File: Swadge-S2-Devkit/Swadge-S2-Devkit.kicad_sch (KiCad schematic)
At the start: 92 parts, among them J1 LED, J2 DEBUG, P1 USB_C_Plug_USB2.0, Q1 PMOS, SW1 TS-1109S-A-A, SW2 TS-1109S-A-A, SW3 TS-1109S-A-A, SW4 TS-1109S-A-A, SW5 TS-1109S-A-A, SW6 TS-1109S-A-A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

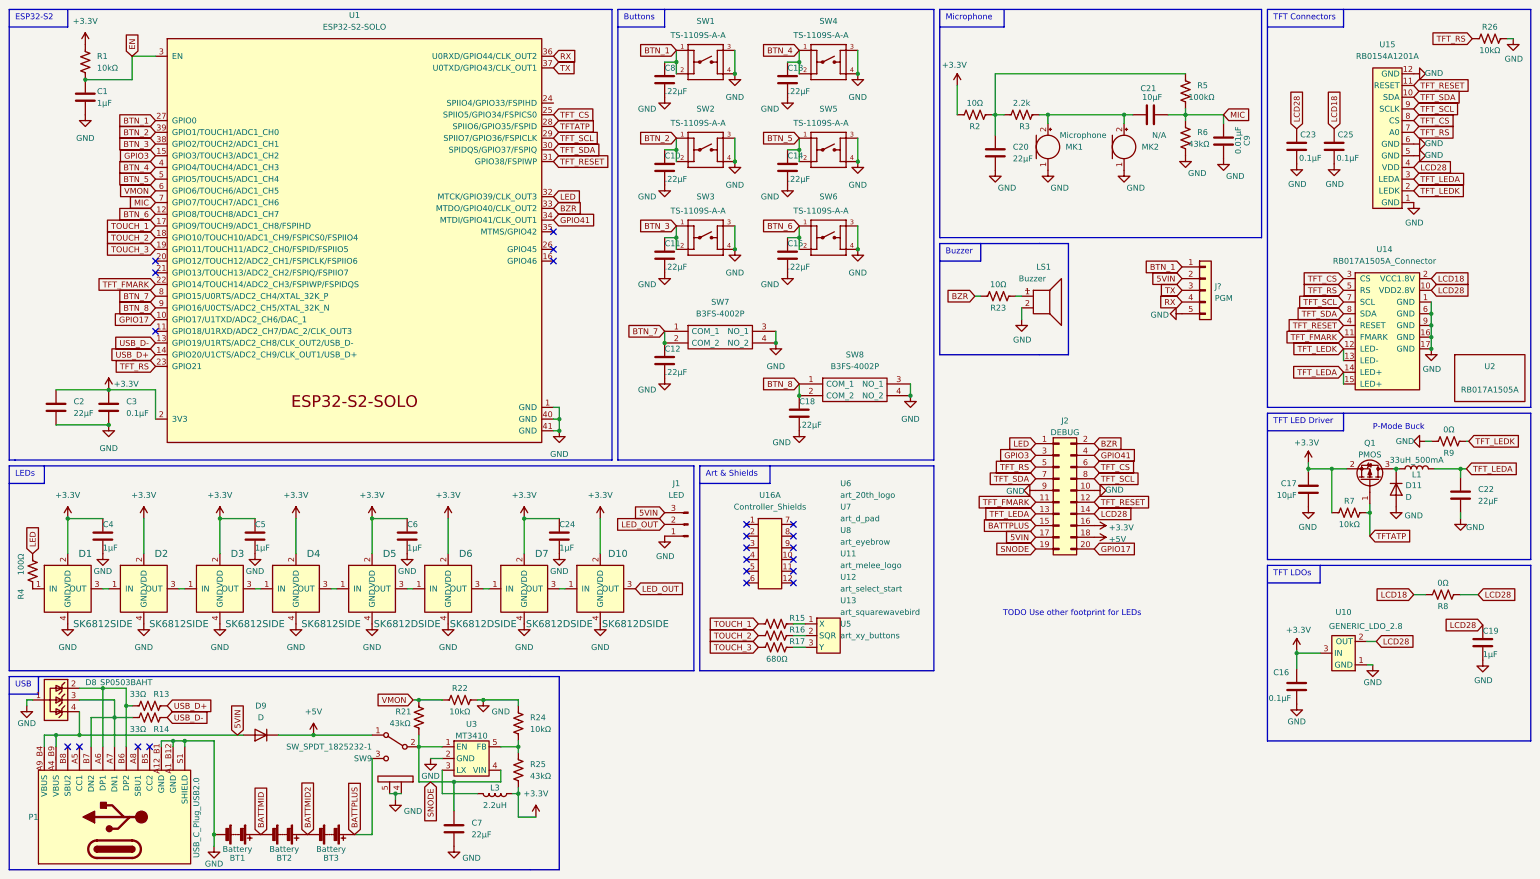
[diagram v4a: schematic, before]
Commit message: Cleaned up part references, BOM
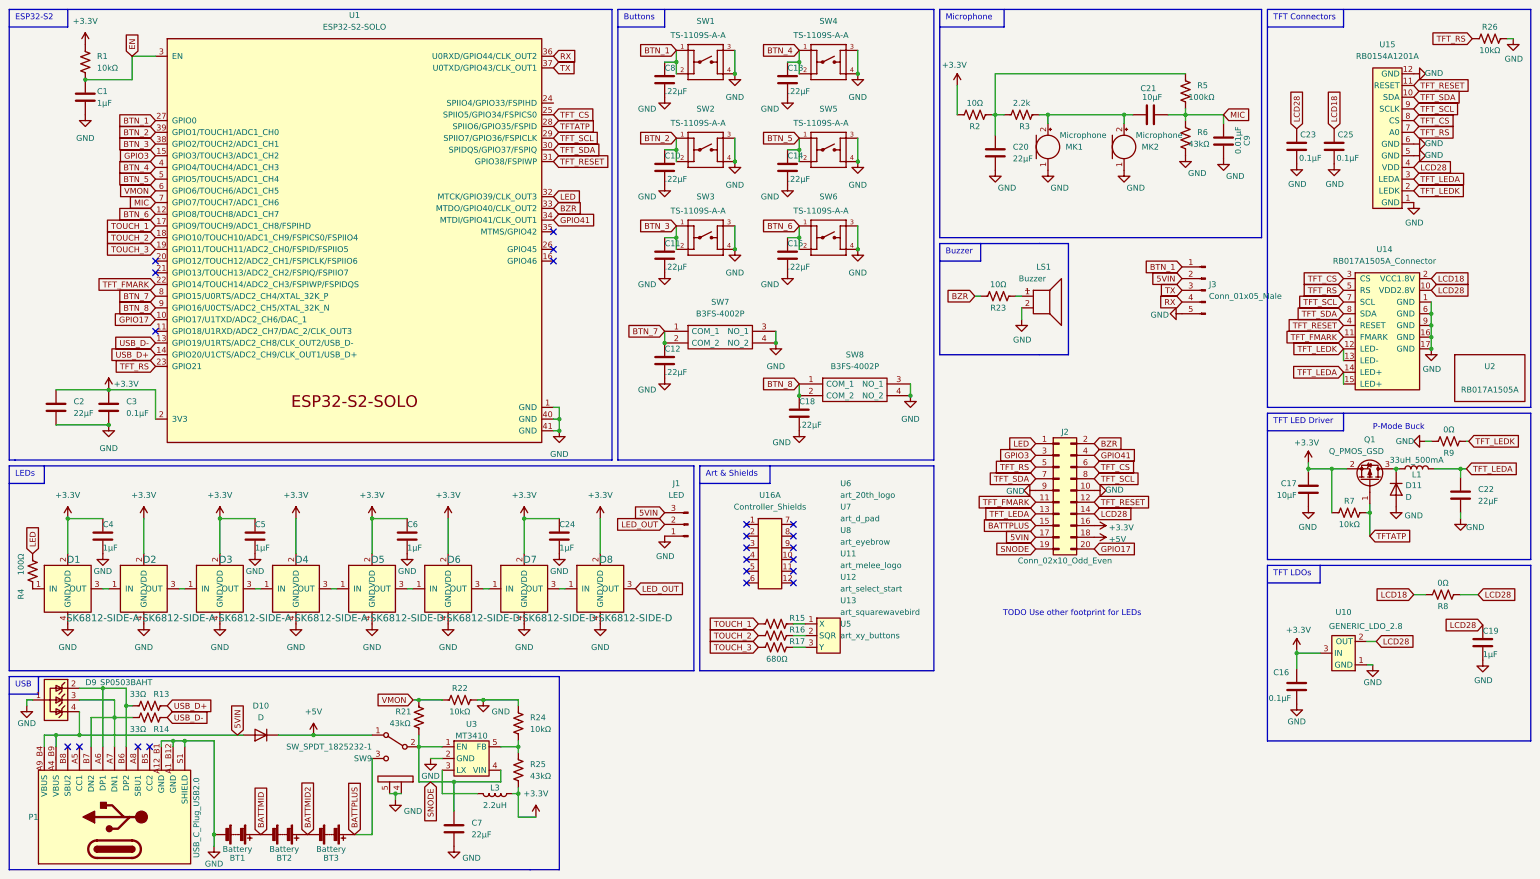
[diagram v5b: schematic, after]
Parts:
- D1, D2, D3, D4: value SK6812SIDE -> SK6812-SIDE-A; symbol Swadge_Parts:SK6812SIDE -> Swadge_Parts:SK6812-SIDE-A
- D5, D6, D7: value SK6812DSIDE -> SK6812-SIDE-D; symbol Swadge_Parts:SK6812SIDE -> Swadge_Parts:SK6812-SIDE-D; Digikey (none) -> 2007-BB-HRGB24R-TRB-BTR-ND; LCSC C2890041 -> C2890037
- D8: renamed from D10; value SK6812DSIDE -> SK6812-SIDE-D; symbol Swadge_Parts:SK6812SIDE -> Swadge_Parts:SK6812-SIDE-D; Digikey (none) -> 2007-BB-HRGB24R-TRB-BTR-ND; LCSC C2890041 -> C2890037
- J1: Notes LED_OUT -> DNP
- J2: value DEBUG -> Conn_02x10_Odd_Even; footprint Connector_PinHeader_2.54mm:PinHeader_2x10_P2.54mm_Vertical -> Swadge_Parts:PinHeader_2x10_P2.54mm_Vertical; symbol Connector_Generic:Conn_02x10_Odd_Even -> Swadge_Parts:Conn_02x10_Odd_Even; LCSC NP -> C492427; Substitutable (none) -> Y
- J3: renamed from J?; value PGM -> Conn_01x05_Male; footprint Connector_PinHeader_2.54mm:PinHeader_1x05_P2.54mm_Vertical -> Swadge_Parts:PinHeader_1x05_P2.54mm_Vertical; symbol Connector_Generic:Conn_01x05 -> Swadge_Parts:Conn_01x05_Male; LCSC NP -> C390683; Substitutable (none) -> Y
- MK1: footprint Swadge_Parts:GOERTEK_MIC_B4013AM423 -> Swadge_Parts:INGHAi GMI6050P-56DB; Cost100 13 -> 70; Digikey N/A -> 102-1721-ND
- MK2: value N/A -> Microphone; footprint Swadge_Parts:INGHAi GMI6050P-56DB -> Swadge_Parts:GOERTEK_MIC_B4013AM423; Cost100 0 -> 0.17; Digikey N/A -> (none); LCSC N/A -> C2835889; Notes (none) -> DNP
- Q1: value PMOS -> Q_PMOS_GSD; footprint Package_TO_SOT_SMD:SOT-23 -> Swadge_Parts:SOT-23; symbol Device:Q_PMOS_GSD -> Swadge_Parts:Q_PMOS_GSD; Substitutable (none) -> Y
- U11, U12, U13, U5, U6, U7, U8: LCSC -- -> (none)
- renumbered D9 to D10, D8 to D9

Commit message: Update design, routed.
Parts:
- removed J1: LED, Swadge_Parts:PinHeader_1x03_P2.54mm_Vertical, symbol Swadge_Parts:Conn_01x03_Male
- added J1: SAO, Connector_PinSocket_2.54mm:PinSocket_2x03_P2.54mm_Vertical, symbol Connector_Generic:Conn_02x03_Odd_Even
- J2: value Conn_02x10_Odd_Even -> DEBUG
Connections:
- net +3V3: now also J1.1 (Pin_1)
- net GND: now also J2.3 (Pin_3), J2.4 (Pin_4), J1.2 (Pin_2)
- net GPIO17: now also J1.6 (Pin_6); no longer J2.20 (Pin_20)
- net GPIO3: now also J1.5 (Pin_5); no longer J2.3 (Pin_3)
- net GPIO41: now also J1.4 (Pin_4); no longer J2.4 (Pin_4)
- net TFTATP: now also J2.20 (Pin_20)
- net at P1.A6 (DP1), P1.B6 (DP2), R13.2: now also D9.3 (K); no longer D9.2 (K)
- net GPIO42: now reaches U1.35 (MTMS/GPIO42)
- net GPIO42: now also J1.3 (Pin_3)
- net at P1.A7 (DN1), P1.B7 (DN2), R14.2: now also D9.2 (K); no longer D9.3 (K)
- net LED_OUT: no longer names the net of D8.3 (OUT)
- no-connect marks 22 -> 21
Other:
- moved on the sheet: J2

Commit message: Clean BOM, update designators, move passives from under batteries, flip mic positions, use parts in Swadge_Parts
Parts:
- ART1: renamed from U6; Notes Not a part, DNP -> DNP, not a component
- ART2: renamed from U7; Notes Not a part, DNP -> DNP, not a component
- ART3: renamed from U8; Notes Not a part, DNP -> DNP, not a component
- ART4: renamed from U11; Notes Not a part, DNP -> DNP, not a component
- ART5: renamed from U12; Notes Not a part, DNP -> DNP, not a component
- ART6: renamed from U5; Notes Not a part, DNP -> DNP, not a component
- ART7: renamed from U13; Notes Not a part, DNP -> DNP, not a component
- J1: footprint Connector_PinSocket_2.54mm:PinSocket_2x03_P2.54mm_Vertical -> Swadge_Parts:PinHeader_2x03_P2.54mm_Vertical; symbol Connector_Generic:Conn_02x03_Odd_Even -> Swadge_Parts:Conn_02x03_Odd_Even; Cost100 (none) -> 0.0109; LCSC N/A -> C402781; Notes (none) -> DNP; Substitutable (none) -> Y
- J2, J3: Notes (none) -> DNP
- U4: renamed from U15; Substitutable (none) -> N
- U6: renamed from U16; Substitutable (none) -> Y
- renumbered U14 to U5, U10 to U7
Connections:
- no-connect marks 21 -> 22
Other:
- note added: "Pin Connectors"
- moved on the sheet: J1, J2, J3

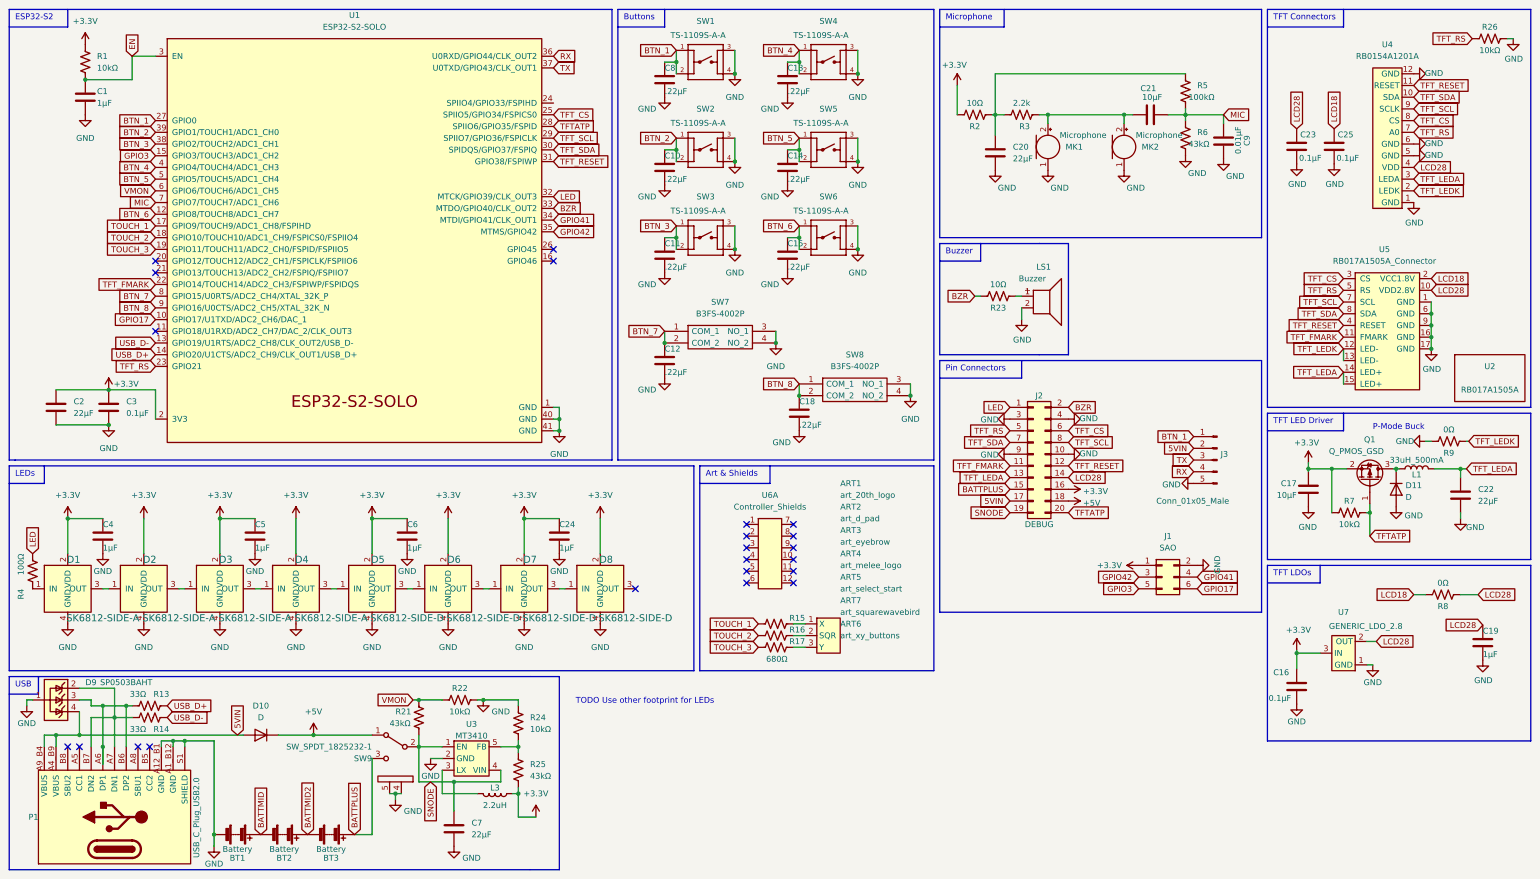
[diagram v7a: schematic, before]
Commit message: Readded accel
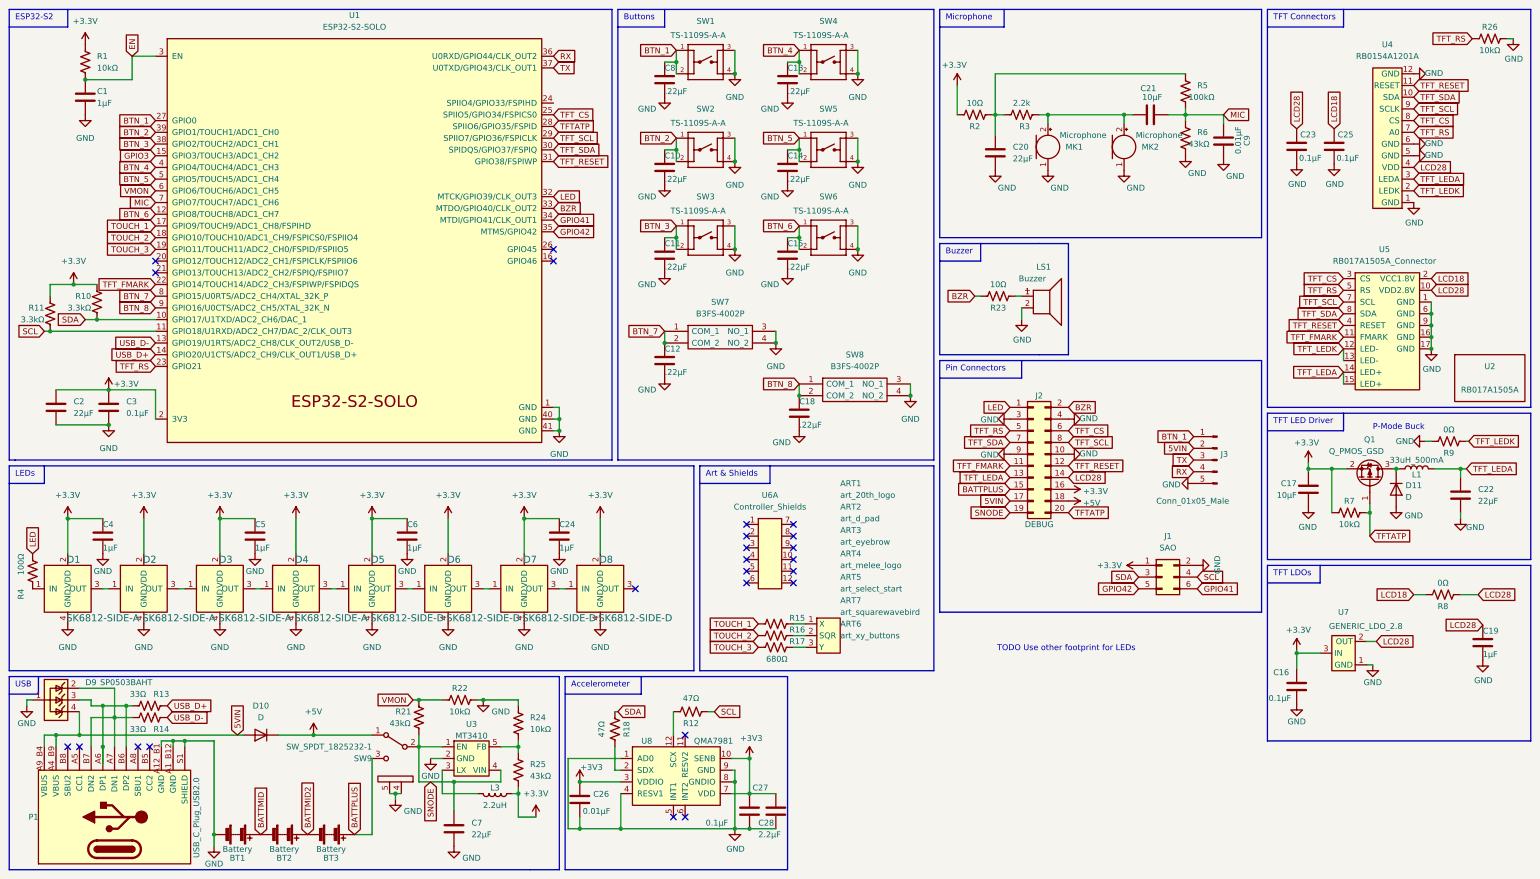
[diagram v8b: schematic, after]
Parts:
- added C26: 0.01μF, Swadge_Parts:C_0603_1608Metric, symbol Swadge_Parts:C
- added C27: 0.1μF, Swadge_Parts:C_0603_1608Metric, symbol Swadge_Parts:C
- added C28: 2.2μF, Swadge_Parts:C_0603_1608Metric, symbol Swadge_Parts:C
- added R10, R11: 3.3kΩ, Swadge_Parts:R_0603_1608Metric, symbol Swadge_Parts:R_US
- added R12, R18: 47Ω, Swadge_Parts:R_0603_1608Metric, symbol Swadge_Parts:R_US
- added U8: QMA7981, Swadge_Parts:QMA6981, symbol Swadge_Parts:QMA7981
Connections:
- net +3V3: now also C26.1, C27.1, C28.1, R10.1, R11.2, U8.10 (SENB), U8.3 (VDDIO), U8.7 (VDD)
- net GND: now also C26.2, C27.2, C28.2, U8.1 (AD0), U8.4 (RESV1), U8.8 (GNDIO), U8.9 (GND)
- net GPIO3: no longer J1.5 (Pin_5)
- net GPIO41: now also J1.6 (Pin_6); no longer J1.4 (Pin_4)
- net GPIO42: now also J1.5 (Pin_5); no longer J1.3 (Pin_3)
- net SCL: now reaches U1.11 (GPIO18/U1RXD/ADC2_CH7/DAC_2/CLK_OUT3)
- net SCL: now also J1.4 (Pin_4), R11.1, R12.1
- net GPIO17 renamed SDA
- net SDA: now also J1.3 (Pin_3), R10.2, R18.1; no longer J1.6 (Pin_6)
- new net: R18.2, U8.2 (SDX)
- new net: R12.2, U8.12 (SCX)
- no-connect marks 22 -> 24
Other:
- note added: "Accelerometer"
